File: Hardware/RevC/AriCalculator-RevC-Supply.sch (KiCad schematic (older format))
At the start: 9 parts, among them IC2 MCP1640, SW1 POWER SWITCH

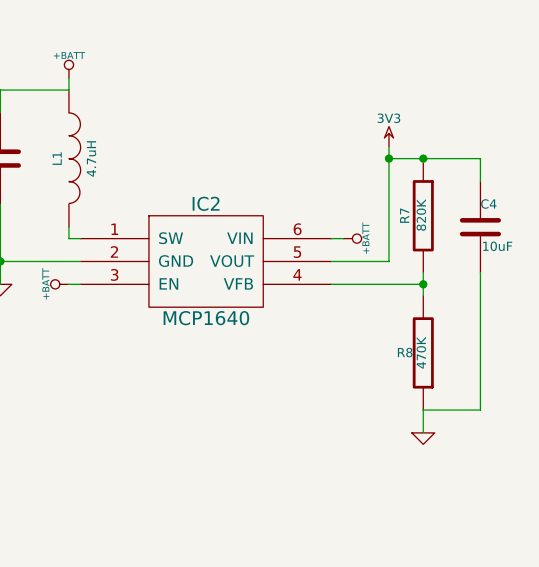
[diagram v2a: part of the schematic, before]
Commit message: started RevC layout
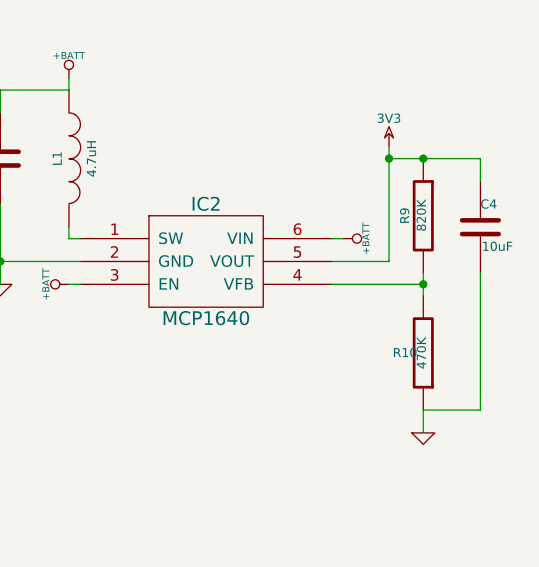
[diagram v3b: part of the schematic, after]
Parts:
- renumbered R8 to R10, R7 to R9
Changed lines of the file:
@@
 $EndComp
 $Comp
-L R R8
+L R R10
 U 1 1 544A8896
 P 5450 3350
-F 0 "R8" H 5530 3350 40  0000 C CNN
+F 0 "R10" H 5530 3350 40  0000 C CNN
 F 1 "470K" V 5457 3351 40  0000 C CNN
 F 2 "~" V 5380 3350 30  0000 C CNN
@@
 $EndComp
 $Comp
-L R R7
+L R R9
 U 1 1 544A88A5
 P 5450 2750
-F 0 "R7" V 5530 2750 40  0000 C CNN
+F 0 "R9" V 5530 2750 40  0000 C CNN
 F 1 "820K" V 5457 2751 40  0000 C CNN
 F 2 "~" V 5380 2750 30  0000 C CNN

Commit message: work in progress
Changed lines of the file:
@@
 Sheet 2 6
 Title "Supply"
-Date "4 nov 2014"
+Date "5 nov 2014"
 Rev "RevC"
 Comp "Dirk Heisswolf"
@@
 F 3 "~" H 2650 2200 60  0000 C CNN
 	1    2650 2200
-	0    1    1    0
+	0    -1   1    0
 $EndComp
 $Comp

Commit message: work in progress
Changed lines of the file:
@@
 Sheet 2 6
 Title "Supply"
-Date "15 nov 2014"
+Date "25 nov 2014"
 Rev "RevC"
 Comp "Dirk Heisswolf"
@@
 F 3 "~" H 2650 2200 60  0000 C CNN
 	1    2650 2200
-	0    -1   1    0
+	0    1    1    0
 $EndComp
 $Comp
